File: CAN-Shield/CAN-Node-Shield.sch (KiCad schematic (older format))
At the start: 24 parts, among them J1 Main_Port, J10 IOH, J2 Daisy-Chain-Port, J3 Sensor, J4 Sensor, J5 Sensor, J6 Sensor, J7 Power, J8 Analog, J9 IOL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

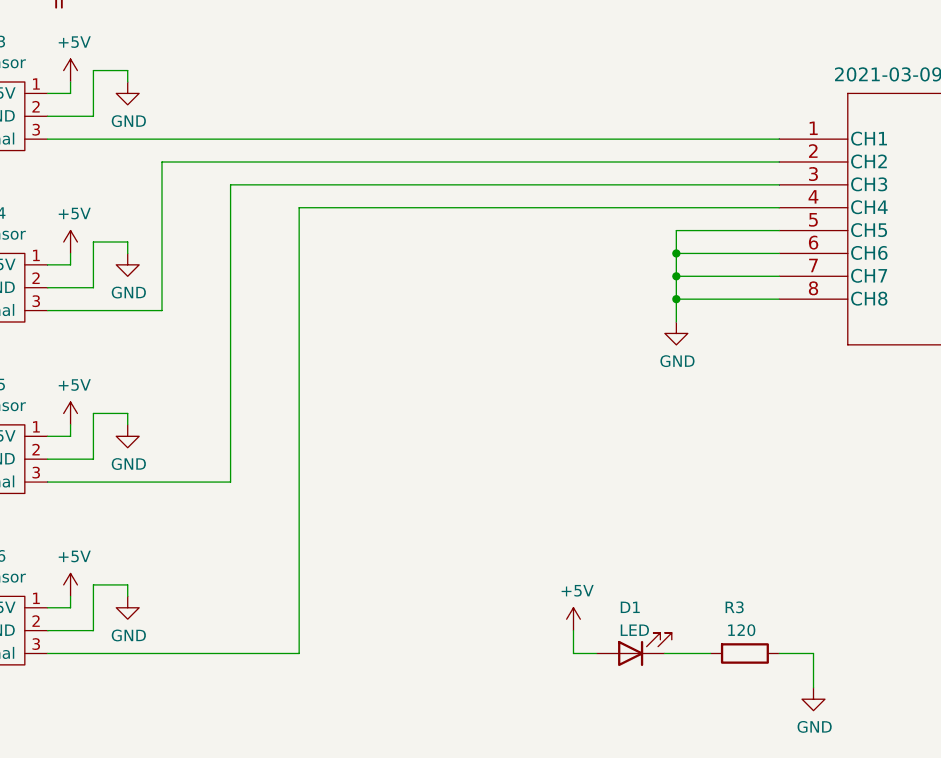
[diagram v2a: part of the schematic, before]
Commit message: Alternated ADC inputs
Changes:
- Changed the ADC input ports to be connected to alternating ADC chip inputs to separate the traces to help reduce potential for cross-talk.
- Increased the width of the trace between the 12V power ports to allow for increased current capacity since this trace will carry power for all downstream devices.
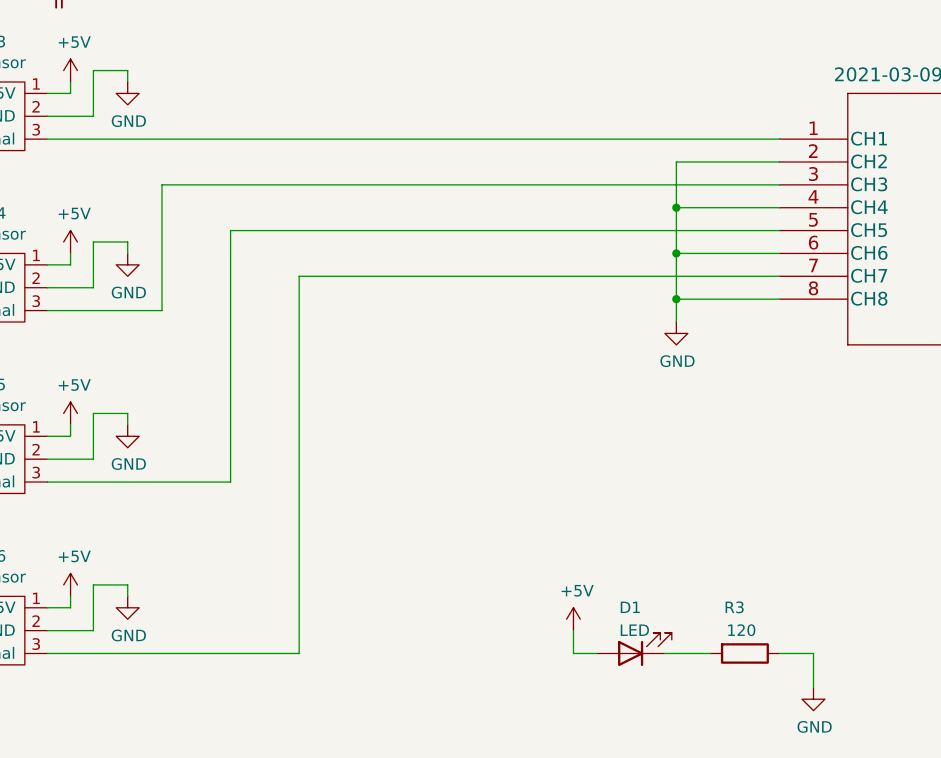
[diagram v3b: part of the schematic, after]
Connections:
- net GND: now also U3.2 (CH2), U3.4 (CH4); no longer U3.5 (CH5), U3.7 (CH7)
- net at J4.3 (Signal): now also U3.3 (CH3); no longer U3.2 (CH2)
- net at J5.3 (Signal): now also U3.5 (CH5); no longer U3.3 (CH3)
- net at J6.3 (Signal): now also U3.7 (CH7); no longer U3.4 (CH4)
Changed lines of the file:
@@
 	9150 2500 9150 4900
-Wire Wire Line
-	2950 4700 2950 5350
-Wire Wire Line
-	3250 4800 3250 6100
-Wire Wire Line
-	3550 4900 3550 6850
 Wire Wire Line
 	3550 2000 5050 2000
@@
 	2450 4600 5650 4600
 Wire Wire Line
-	2950 4700 5650 4700
-Wire Wire Line
-	3250 4800 5650 4800
-Wire Wire Line
-	3550 4900 5650 4900
+	2950 4800 5650 4800
+Wire Wire Line
+	3250 5000 5650 5000
+Wire Wire Line
+	3550 5200 5650 5200
 Wire Wire Line
 	8050 2100 8400 2100
@@
 	1    0    0    -1
 $EndComp
-Wire Wire Line
-	5650 5000 5200 5000
-Wire Wire Line
-	5200 5000 5200 5100
-Wire Wire Line
-	5650 5100 5200 5100
-Connection ~ 5200 5100
-Wire Wire Line
-	5200 5100 5200 5200
-Wire Wire Line
-	5650 5200 5200 5200
-Connection ~ 5200 5200
-Wire Wire Line
-	5200 5200 5200 5300
-Wire Wire Line
-	5650 5300 5200 5300
-Connection ~ 5200 5300
-Wire Wire Line
-	5200 5300 5200 5400
 $Comp
 L CAN-Node-Shield-rescue:2021-03-09_22-56-21_MCP2515-I_P-CAN-Node-Shield-cache U2
@@
 Wire Wire Line
 	9000 3300 10000 3300
+Wire Wire Line
+	2950 4800 2950 5350
+Wire Wire Line
+	5650 4700 5200 4700
+Wire Wire Line
+	5200 4700 5200 4900
+Wire Wire Line
+	3550 5200 3550 6850
+Wire Wire Line
+	3250 5000 3250 6100
+Wire Wire Line
+	5650 5300 5200 5300
+Connection ~ 5200 5300
+Wire Wire Line
+	5200 5300 5200 5400
+Wire Wire Line
+	5200 5100 5650 5100
+Connection ~ 5200 5100
+Wire Wire Line
+	5200 5100 5200 5300
+Wire Wire Line
+	5650 4900 5200 4900
+Connection ~ 5200 4900
+Wire Wire Line
+	5200 4900 5200 5100
 $EndSCHEMATC
